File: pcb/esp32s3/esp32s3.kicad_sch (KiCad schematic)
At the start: 25 parts, among them SW1 BOOT, U1 ESP32-S3FN8, U9 2450AT18D0100E, X1 40MHz

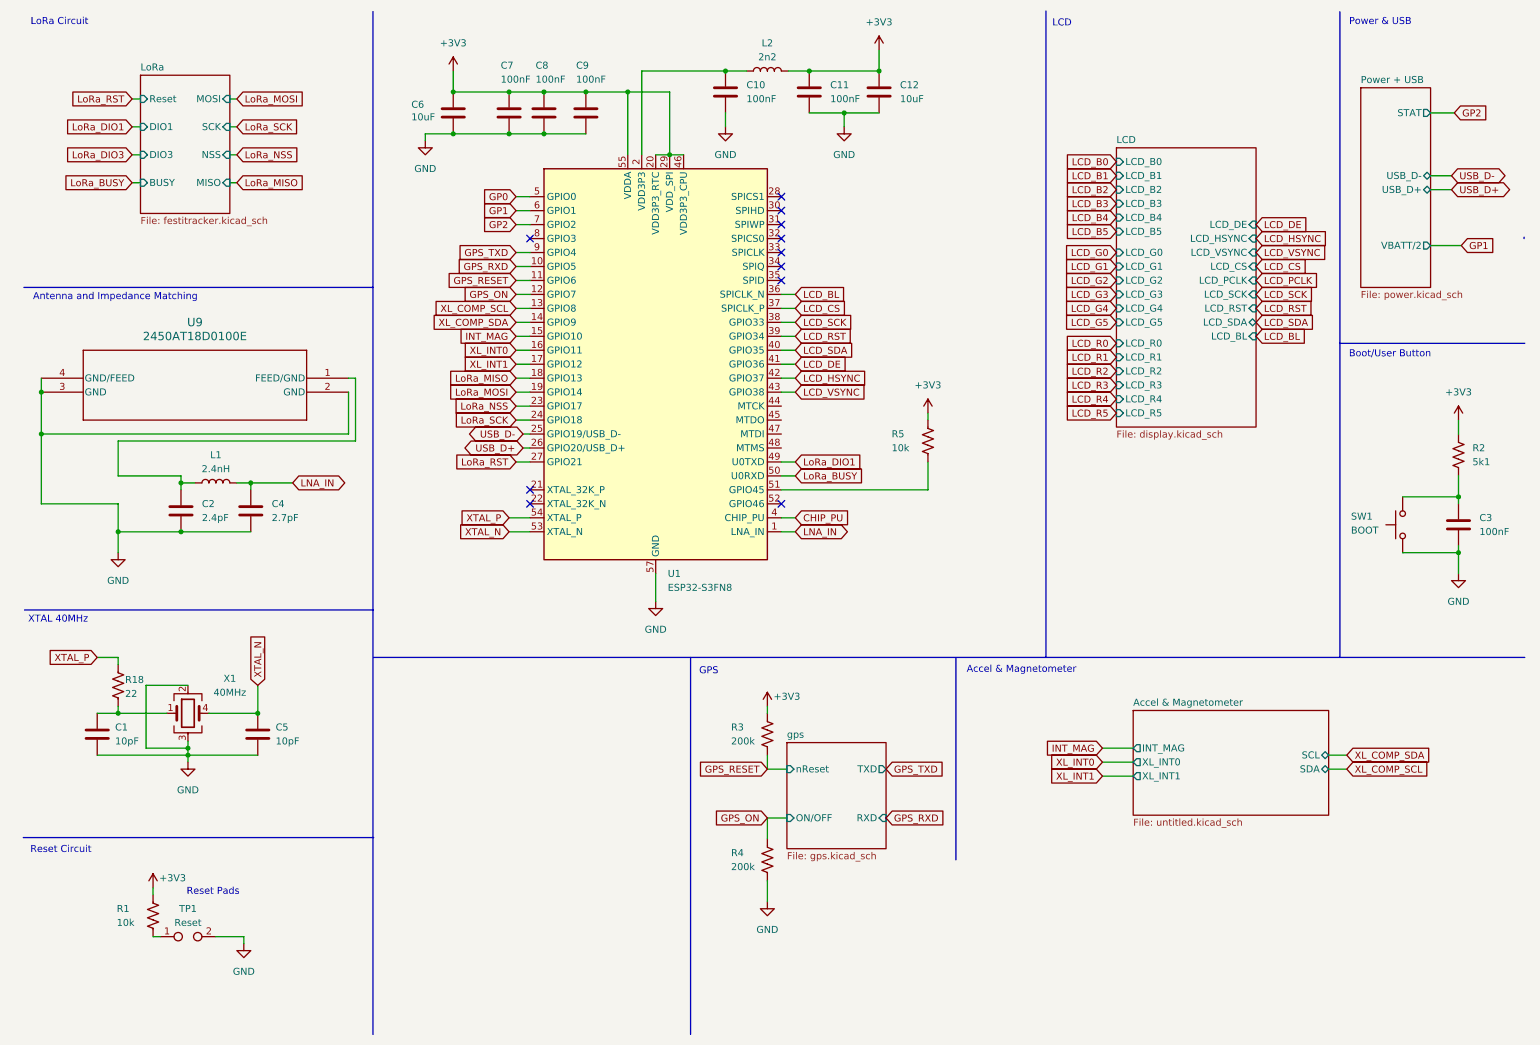
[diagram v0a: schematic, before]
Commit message: Update PCB with new components and footprints
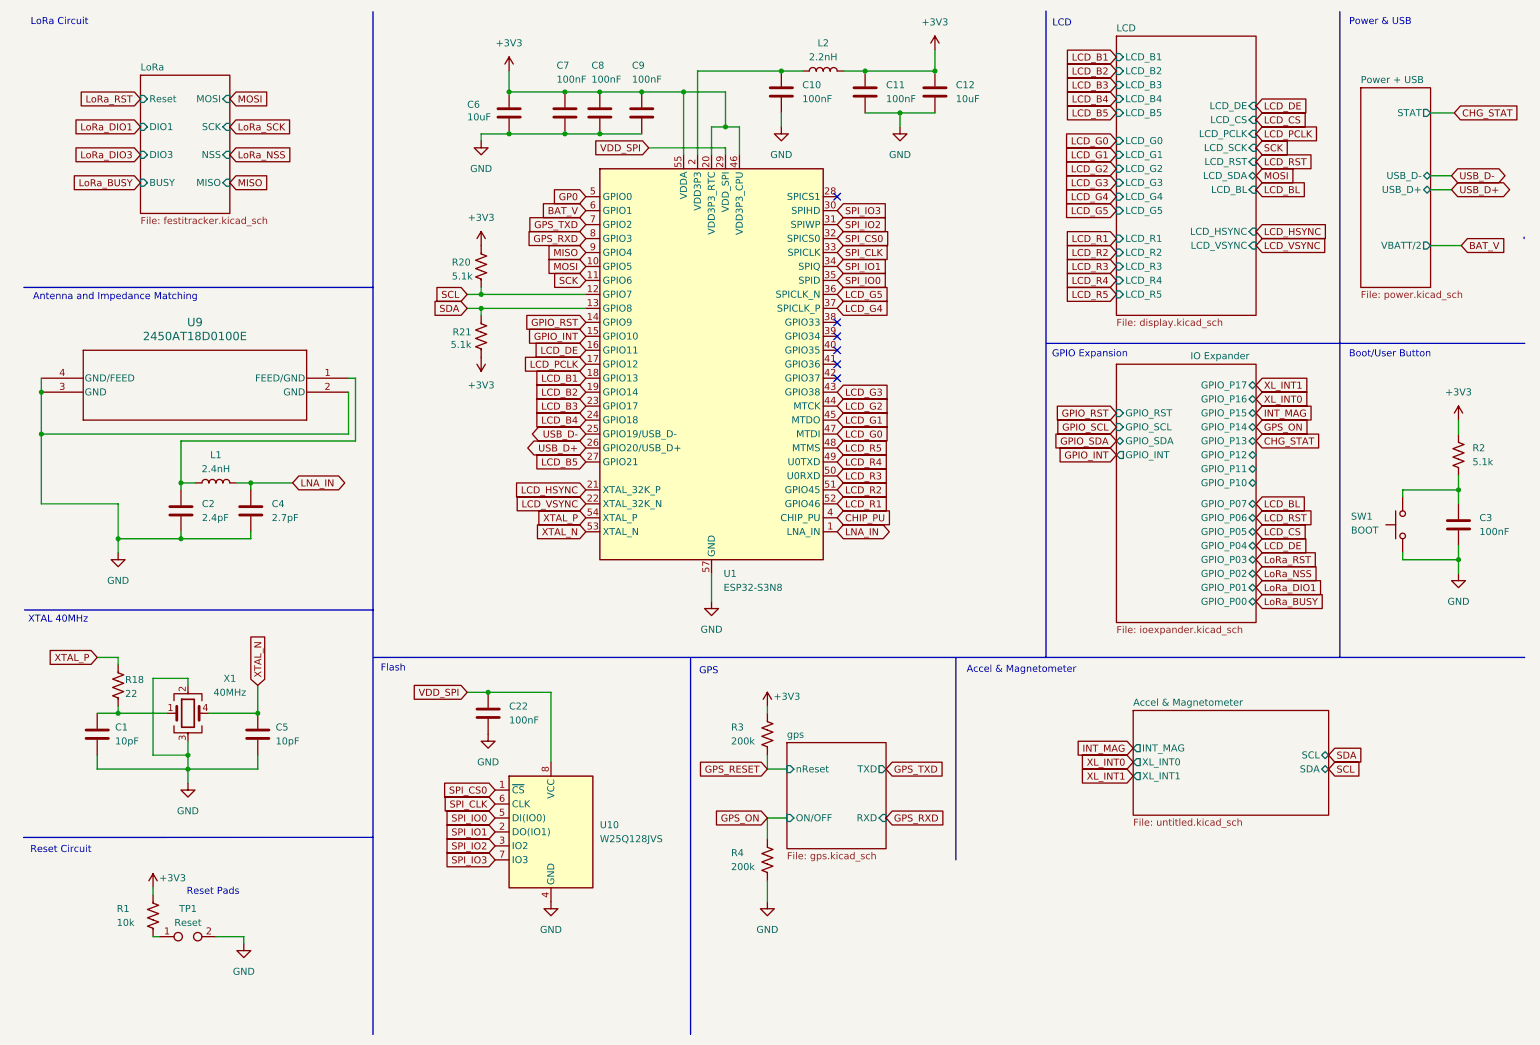
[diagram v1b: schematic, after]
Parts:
- removed R5: 10k, Resistor_SMD:R_0402_1005Metric, symbol Device:R_US
- added C22: 100nF, Capacitor_SMD:C_0402_1005Metric, symbol Device:C
- added R20, R21: 5.1k, Resistor_SMD:R_0402_1005Metric, symbol Device:R_US
- added U10: W25Q128JVS, Package_SO:SOIC-8_5.23x5.23mm_P1.27mm, symbol Memory_Flash:W25Q128JVS
- L2: value 2n2 -> 2.2nH
- R2: value 5k1 -> 5.1k
- SW1: footprint Button_Switch_SMD:SW_MEC_5GSH9 -> custom_comps:vert_button_6mm
- U1: value ESP32-S3FN8 -> ESP32-S3N8
- U9: footprint 2450AT18D0100E:2450AT18D0100E_JOT -> custom_comps:2450AT18D0100E_JOT
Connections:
- net GP2 is gone; now on net GPS_TXD: U1.7 (GPIO2)
- net LoRa_MISO is gone; now on net LCD_B1: U1.18 (GPIO13)
- net LoRa_MOSI is gone; now on net LCD_B2: U1.19 (GPIO14)
- net +3V3: now also R20.1, R21.1; no longer U1.29 (VDD_SPI)
- net GND: now also C22.2, U10.4 (GND)
- net GPS_ON: no longer U1.12 (GPIO7)
- net GPS_RESET: no longer U1.11 (GPIO6)
- net GPS_RXD: now also U1.8 (GPIO3); no longer U1.10 (GPIO5)
- net GPS_TXD: no longer U1.9 (GPIO4)
- net INT_MAG: no longer U1.15 (GPIO10)
- net LCD_B3: now also U1.23 (GPIO17)
- net LCD_B4: now also U1.24 (GPIO18)
- net LCD_B5: now also U1.27 (GPIO21)
- net LCD_BL: no longer U1.36 (SPICLK_N)
- net LCD_CS: no longer U1.37 (SPICLK_P)
- net LCD_DE: now also U1.16 (GPIO11); no longer U1.41 (GPIO36)
- net LCD_G0: now also U1.47 (MTDI)
- net LCD_G1: now also U1.45 (MTDO)
- net LCD_G2: now also U1.44 (MTCK)
- net LCD_G3: now also U1.43 (GPIO38)
- net LCD_G4: now also U1.37 (SPICLK_P)
- net LCD_G5: now also U1.36 (SPICLK_N)
- net LCD_HSYNC: now also U1.21 (XTAL_32K_P); no longer U1.42 (GPIO37)
- net LCD_PCLK: now also U1.17 (GPIO12)
- net LCD_R1: now also U1.52 (GPIO46)
- net LCD_R2: now also U1.51 (GPIO45)
- net LCD_R3: now also U1.50 (U0RXD)
- net LCD_R4: now also U1.49 (U0TXD)
- net LCD_R5: now also U1.48 (MTMS)
- net LCD_RST: no longer U1.39 (GPIO34)
- net LCD_VSYNC: now also U1.22 (XTAL_32K_N); no longer U1.43 (GPIO38)
- net LoRa_BUSY: no longer U1.50 (U0RXD)
- net LoRa_DIO1: no longer U1.49 (U0TXD)
- net LoRa_NSS: no longer U1.23 (GPIO17)
- net LoRa_RST: no longer U1.27 (GPIO21)
- net LoRa_SCK: no longer U1.24 (GPIO18)
- net XL_INT0: no longer U1.16 (GPIO11)
- net XL_INT1: no longer U1.17 (GPIO12)
- net SPI_IO3: now reaches U1.30 (SPIHD)
- net SPI_IO3: now also U10.7 (IO3)
- net SPI_IO2: now reaches U1.31 (SPIWP)
- net SPI_IO2: now also U10.3 (IO2)
- net SPI_CS0: now reaches U1.32 (SPICS0)
- net SPI_CS0: now also U10.1 (~{CS})
- net SPI_CLK: now reaches U1.33 (SPICLK)
- net SPI_CLK: now also U10.6 (CLK)
- net SPI_IO1: now reaches U1.34 (SPIQ)
- net SPI_IO1: now also U10.2 (DO(IO1))
- net SPI_IO0: now reaches U1.35 (SPID)
- net SPI_IO0: now also U10.5 (DI(IO0))
- net GP1 renamed BAT_V
- net LCD_SCK: no longer names the net of U1.38 (GPIO33)
- net LCD_SDA: no longer names the net of U1.40 (GPIO35)
- net XL_COMP_SCL renamed SDA
- net SDA: now also R21.2
- net XL_COMP_SDA renamed GPIO_RST
- new net GPIO_INT: U1.15 (GPIO10)
- new net MISO: U1.9 (GPIO4)
- new net MOSI: U1.10 (GPIO5)
- new net SCK: U1.11 (GPIO6)
- new net SCL: R20.2, U1.12 (GPIO7)
- new net VDD_SPI: C22.1, U1.29 (VDD_SPI), U10.8 (VCC)
- no-connect marks 11 -> 6
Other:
- added sheet IO Expander (ioexpander.kicad_sch)
- sheet LCD ports: added none; removed LCD_B0, LCD_R0
- note added: "Flash"
- note added: "GPIO Expansion"
- moved on the sheet: C10, C11, C12, C6, C7, C8, C9, L2, U1

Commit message: pcb kinda almost done!
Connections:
- net BAT_V: now also U1.15 (GPIO10); no longer U1.6 (GPIO1)
- net GP0: now also C3.1, R2.2, SW1.2
- net GPIO_INT: now also U1.24 (GPIO18); no longer U1.15 (GPIO10)
- net GPIO_RST: now also U1.27 (GPIO21); no longer U1.14 (GPIO9)
- net GPS_RXD: now also U1.47 (MTDI); no longer U1.8 (GPIO3)
- net GPS_TXD: now also U1.48 (MTMS); no longer U1.7 (GPIO2)
- net LCD_B1: now also U1.6 (GPIO1); no longer U1.18 (GPIO13)
- net LCD_B2: now also U1.7 (GPIO2); no longer U1.19 (GPIO14)
- net LCD_B3: now also U1.8 (GPIO3); no longer U1.23 (GPIO17)
- net LCD_B4: now also U1.9 (GPIO4); no longer U1.24 (GPIO18)
- net LCD_B5: now also U1.10 (GPIO5); no longer U1.27 (GPIO21)
- net LCD_DE: now also U1.50 (U0RXD); no longer U1.16 (GPIO11)
- net LCD_G0: now also U1.11 (GPIO6); no longer U1.47 (MTDI)
- net LCD_G1: now also U1.12 (GPIO7); no longer U1.45 (MTDO)
- net LCD_G2: now also U1.13 (GPIO8); no longer U1.44 (MTCK)
- net LCD_G3: now also U1.14 (GPIO9); no longer U1.43 (GPIO38)
- net LCD_G4: now also U1.16 (GPIO11); no longer U1.37 (SPICLK_P)
- net LCD_G5: now also U1.17 (GPIO12); no longer U1.36 (SPICLK_N)
- net LCD_HSYNC: now also U1.52 (GPIO46); no longer U1.21 (XTAL_32K_P)
- net LCD_PCLK: now also U1.49 (U0TXD); no longer U1.17 (GPIO12)
- net LCD_R1: now also U1.18 (GPIO13); no longer U1.52 (GPIO46)
- net LCD_R2: now also U1.19 (GPIO14); no longer U1.51 (GPIO45)
- net LCD_R3: now also U1.21 (XTAL_32K_P); no longer U1.50 (U0RXD)
- net LCD_R4: now also U1.22 (XTAL_32K_N); no longer U1.49 (U0TXD)
- net LCD_R5: now also U1.23 (GPIO17); no longer U1.48 (MTMS)
- net LCD_VSYNC: now also U1.51 (GPIO45); no longer U1.22 (XTAL_32K_N)
- net MISO: now also U1.44 (MTCK); no longer U1.9 (GPIO4)
- net MOSI: now also U1.43 (GPIO38); no longer U1.10 (GPIO5)
- net SCK: now also U1.45 (MTDO); no longer U1.11 (GPIO6)
- net SCL: now also U1.37 (SPICLK_P); no longer U1.12 (GPIO7)
- net SDA: now also U1.36 (SPICLK_N); no longer U1.13 (GPIO8)
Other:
- sheet Accel & Magnetometer ports: added CS_MAG, CS_XL; removed none

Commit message: finishing touches
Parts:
- removed R20, R21: 5.1k, Resistor_SMD:R_0402_1005Metric, symbol Device:R_US
- removed TP1: Reset, Connector_PinHeader_1.00mm:PinHeader_1x02_P1.00mm_Horizontal, symbol Connector:TestPoint_2Pole
- added SW2: PTS815 SJM 250 SMTR LFS, SW4_PTS815 SJM 250 SMTR LFS_CNK, symbol PTS815_SJM_250_SMTR_LFS:PTS815_SJM_250_SMTR_LFS
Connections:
- net +3V3: now also R1.2; no longer R1.1
- net CHIP_PU: now also R1.1, SW2.1 (2)
- net GND: now also SW2.2 (4)
- no-connect marks 6 -> 8
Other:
- sheet LCD ports: added LCD_MOSI; removed LCD_SDA
- note removed: "Reset Pads"
- moved on the sheet: R1

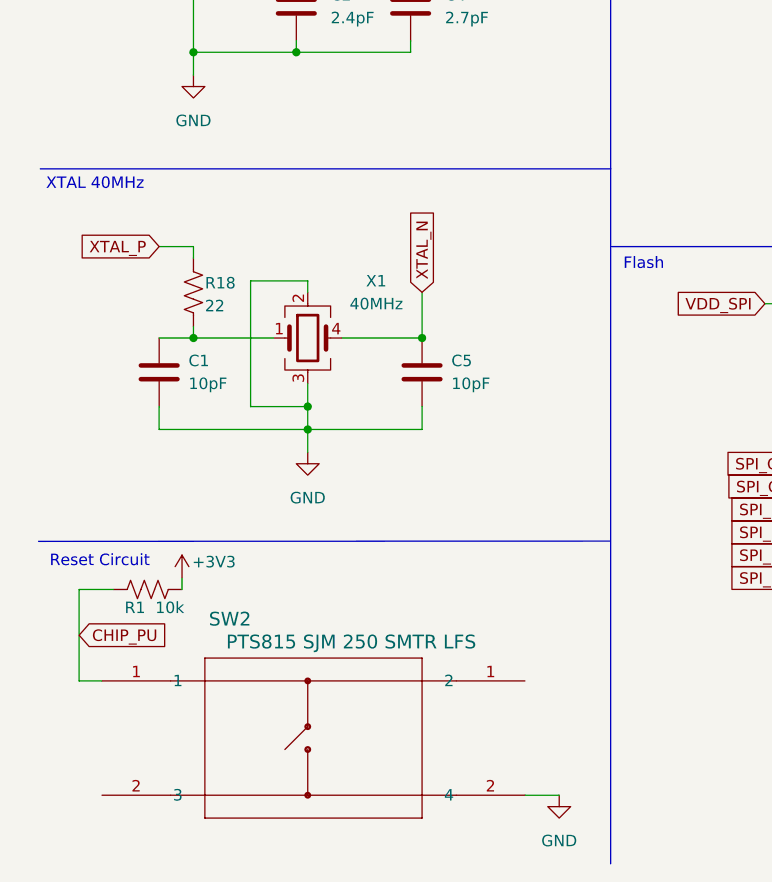
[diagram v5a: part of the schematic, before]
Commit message: added "stm32h7" new pcb and docs
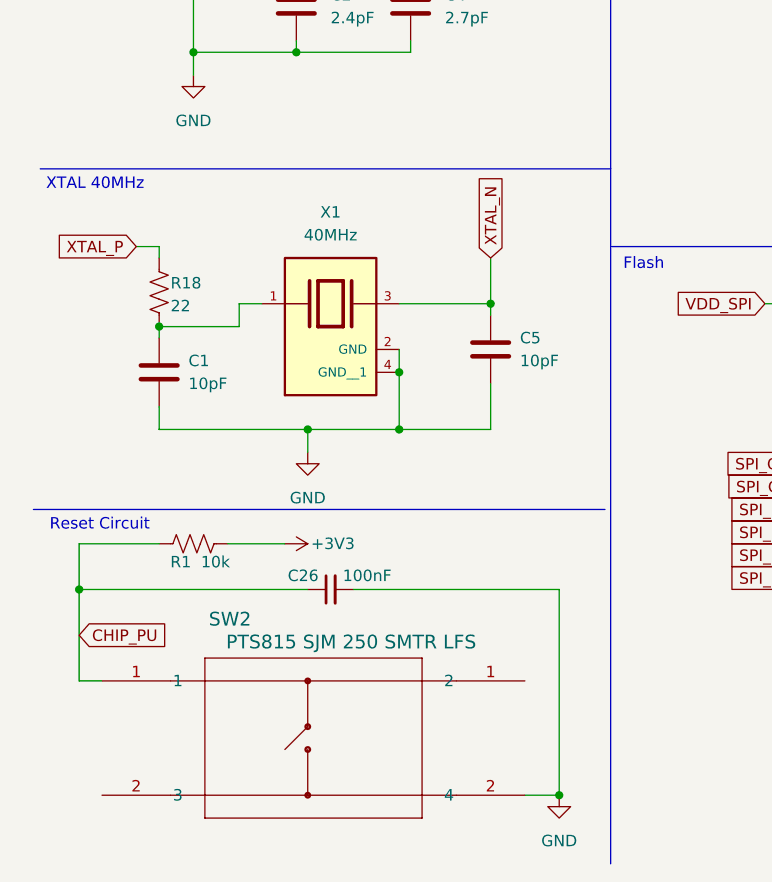
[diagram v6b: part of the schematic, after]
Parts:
- added C26: 100nF, Capacitor_SMD:C_0402_1005Metric, symbol Device:C_Small
- X1: footprint Crystal:Crystal_SMD_Abracon_ABM10-4Pin_2.5x2.0mm -> custom_comps:XTAL_ABM10-40.000MHZ-D30-T3; symbol Device:Crystal_GND23 -> ABM10-40.000MHZ-D30-T3:ABM10-40.000MHZ-D30-T3; MANUFACTURER (none) -> Abracon; MAXIMUM_PACKAGE_HEIGHT (none) -> 0.7 mm; PARTREV (none) -> 04.21.15; STANDARD (none) -> Manufacturer Recommendations
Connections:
- net CHIP_PU: now also C26.1
- net GND: now also X1.4 (GND__1), C26.2; no longer X1.3
- net XTAL_N: now also X1.3; no longer X1.4
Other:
- moved on the sheet: C5, R1, R18
